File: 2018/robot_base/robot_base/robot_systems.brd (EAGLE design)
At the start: 102.8 x 91.4 mm, 92 parts, among them IC1 DRV8840PWP, IC1_C1 0.01uF, IC1_C2 0.1uF, IC1_C3 0.1uF, IC1_C4 0.1uF, IC1_C5 100uF, IC1_C6 470nF, IC1_R1 ???, IC1_R2 ???, IC1_R3 10k, IC1_R4 100m, IC1_R5 1M, IC2 DRV8840PWP, IC2_C1 0.01uF, IC2_C2 0.1uF, IC2_C3 0.1uF, IC2_C4 0.1uF, IC2_C5 100uF, IC2_C6 470nF, IC2_R1 ???, IC2_R2 ???, IC2_R3 10k, IC2_R4 100m, IC2_R5 1M, IC3 DRV8840PWP, IC3_C1 0.01uF, IC3_C2 0.1uF, IC3_C3 0.1uF, IC3_C4 0.1uF, IC3_C5 100uF, IC3_C6 470nF, IC3_R1 ???, IC3_R2 ???, IC3_R3 10k, IC3_R4 100m, IC3_R5 1M

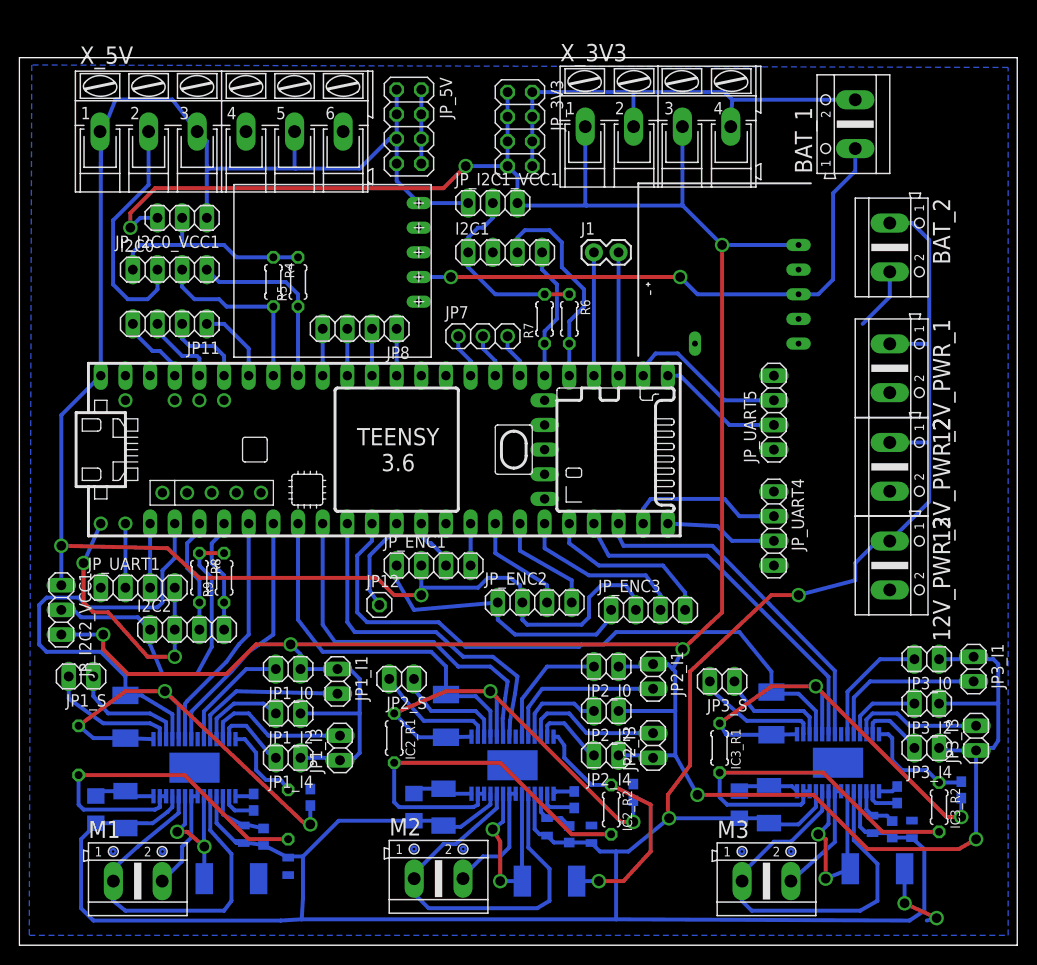
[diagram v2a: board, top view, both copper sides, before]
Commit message: [robot_base] Update robot_base and robot_systems boards.
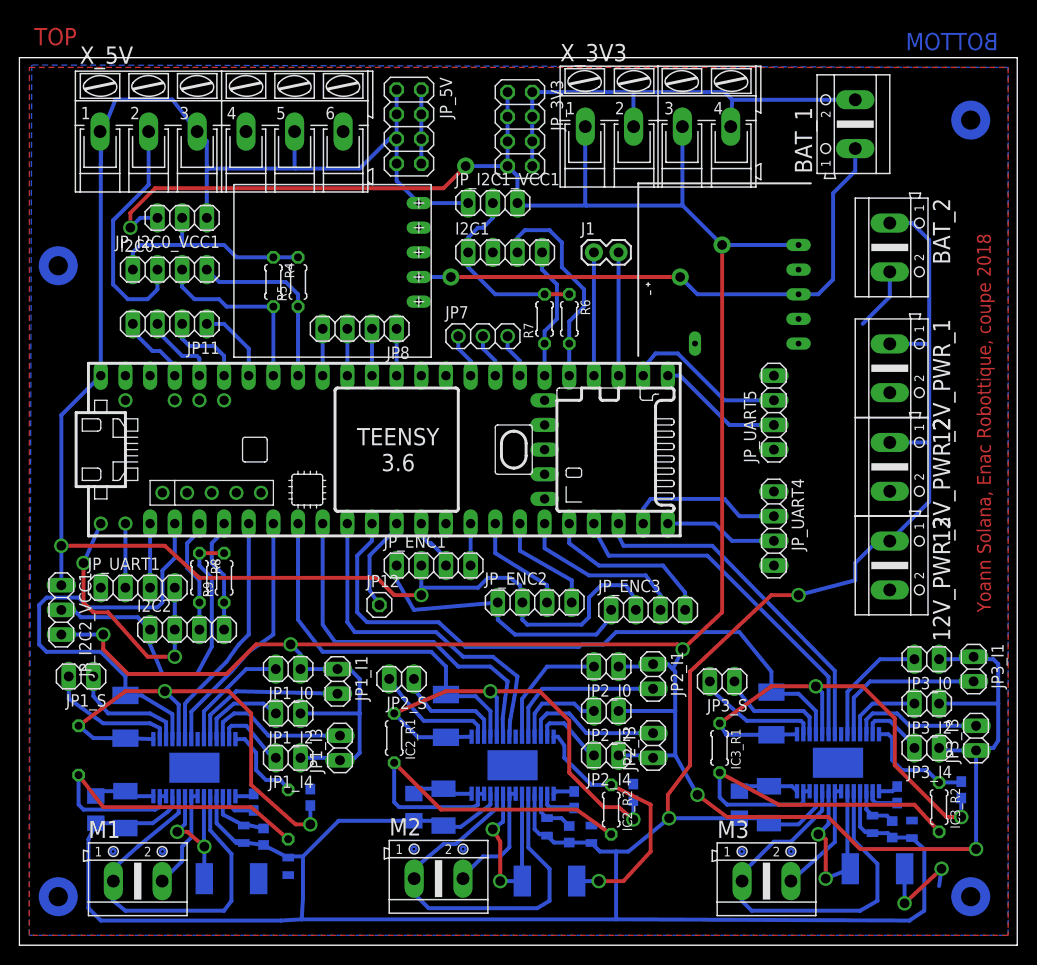
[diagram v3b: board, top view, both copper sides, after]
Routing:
- net IC1_V3P3: track 46.2 -> 51.1 mm
- net IC3_V3P3: track 47.5 -> 50.3 mm
- net IC2_V3P3: track 46.8 -> 49.5 mm
- net GND: track 218.7 -> 221.0 mm
- net 12V2: track 301.8 -> 300.6 mm
- net 3V3: track 347.1 -> 347.7 mm
- added copper zone on layer 1, net GND
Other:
- board text added: "BOTTOM"
- board text added: "TOP"
- board text added: "Yoann Solana, Enac Robottique, coupe 2018"

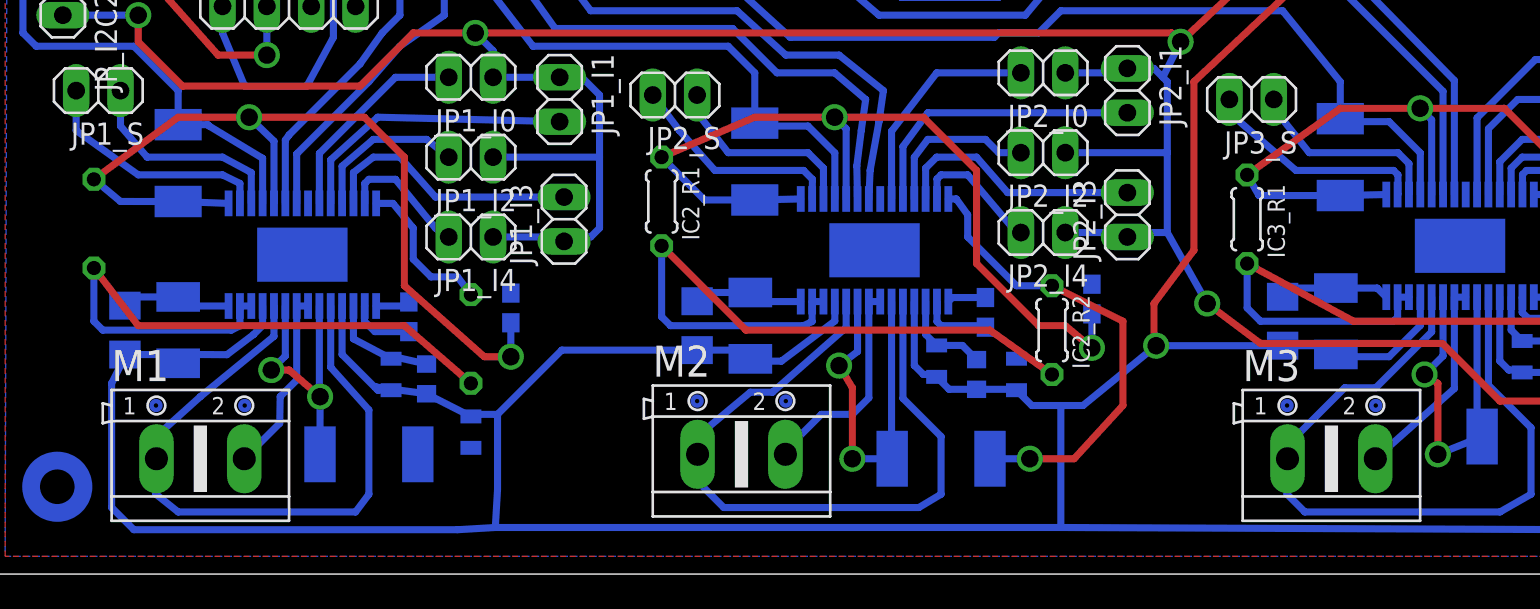
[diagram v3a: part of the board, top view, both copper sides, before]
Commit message: [robot_system] Increase clearance, update package of one condo
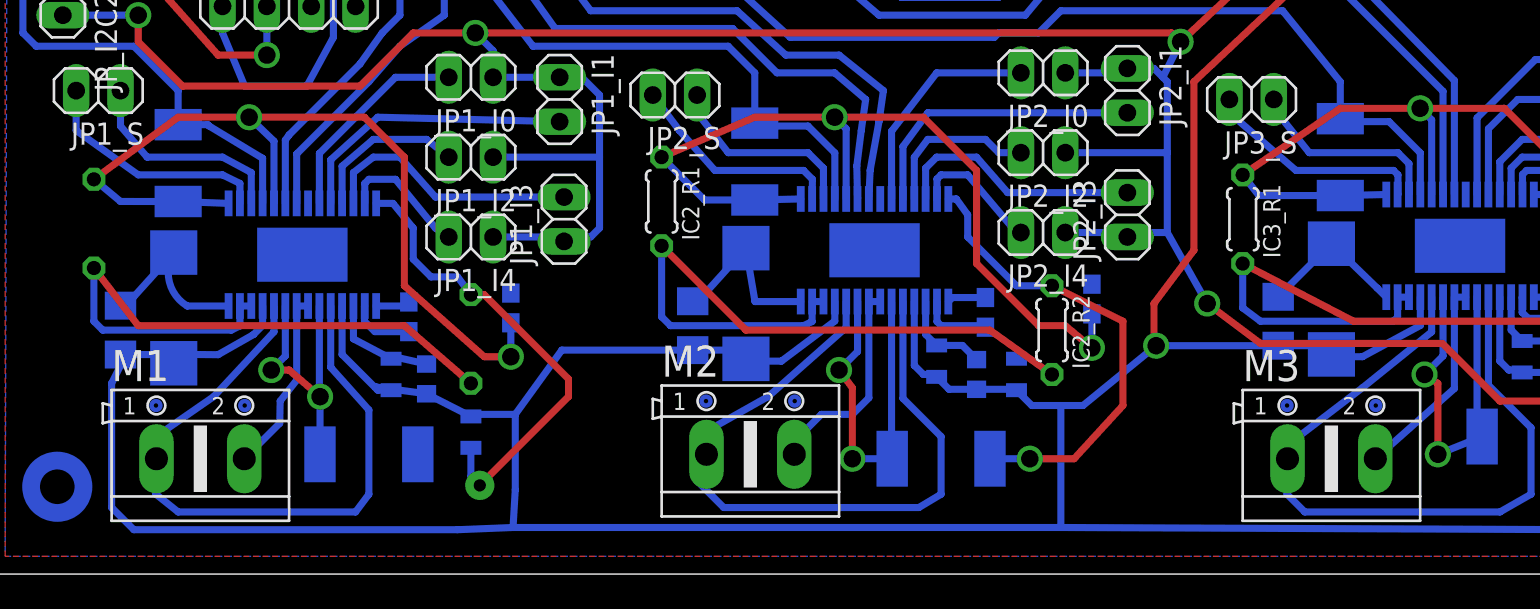
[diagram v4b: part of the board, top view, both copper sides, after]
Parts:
- IC1_C5, IC2_C5, IC3_C5: device SparkFun-Passives:EIA3528-KIT -> SparkFun-Passives:EIA7343
- moved IC2_C5 1.30 mm to (43.4, 15.5)
- moved IC1_C5 1.30 mm to (10.7, 15.2)
- moved IC3_C5 1.30 mm to (77.0, 15.7)
- moved M2 0.51 mm to (43.7, 6.86)
- moved IC3_C4 0.25 mm to (73.9, 14.5)
- moved IC1_C4 0.25 mm to (7.62, 14.0)
- moved IC2_C4 0.25 mm to (40.4, 14.2)
- moved IC3_R1 0.25 mm to (71.9, 20.3)
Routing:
- net GND: track 221.0 -> 248.5 mm, vias 5 -> 6
- net M2_1: track 41.6 -> 42.4 mm
- net 12V2: track 300.6 -> 301.1 mm

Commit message: Debut test motor control
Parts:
- removed 12V_PWR_1, 12V_PWR_2, 12V_PWR_3, BAT_1, BAT_2, M2, M3: (no value), con-ptr500:AK500/2
- removed D24V22F3: D24V22F3, D24V22F3:D24V22F3
- removed D24V50F5: D24V50F5, D24V50F5:D24V50F5
- removed I2C0, I2C1, I2C2, JP11, JP8, JP_ENC1, JP_ENC2, JP_ENC3, JP_UART1, JP_UART4, JP_UART5: (no value), pinhead:1X04
- removed IC2, IC3: DRV8840PWP, DRV8840PWP:SOP65P640X120-29N
- removed IC2_C1, IC3_C1: 0.01uF, rcl:C0603
- removed IC2_C2, IC2_C3, IC3_C2, IC3_C3: 0.1uF, SparkFun-Passives:0805
- removed IC2_C4, IC3_C4: 0.1uF, SparkFun-Passives:1206
- removed IC2_C5, IC3_C5: 100uF, SparkFun-Passives:EIA7343
- removed IC2_C6, IC3_C6: 470nF, rcl:C0603
- removed IC2_R1, IC2_R2, IC3_R1, IC3_R2: ???, resistor:0204/5
- removed IC2_R3, IC3_R3: 10k, rcl:R2010
- removed IC2_R4, IC3_R4: 100m, rcl:R2512
- removed IC2_R5, IC3_R5: 1M, rcl:R0603
- removed J1: (no value), SparkFun-Connectors:1X02
- removed JP12: (no value), pinhead:1X01
- removed JP1_I0, JP1_I1, JP1_I2, JP1_I3, JP1_I4, JP1_S, JP2_I0, JP2_I1, JP2_I2, JP2_I3, JP2_I4, JP2_S, JP3_I0, JP3_I1, JP3_I2, JP3_I3, JP3_I4, JP3_S: (no value), pinhead:1X02
- removed JP7: (no value), adafruit:1X03
- removed JP_3V3, JP_5V: (no value), pinhead:2X04
- removed JP_I2C0_VCC1, JP_I2C1_VCC1, JP_I2C2_VCC1: (no value), pinhead:1X03
- removed R4, R5, R6, R7, R8, R9: (no value), rcl:0204/5
- removed U$1: TEENSY_3.5/3.6TEENSY_3.5/3.6_LONG_PADS, Teensy356:TEENSY_3.5/3.6
- removed X_3V3: (no value), con-ptr500:AK300/4
- removed X_5V: (no value), con-ptr500:AK300/6
- added JP1: (no value), pinhead:1X06
- added JP2: (no value), pinhead:1X04
- added JP3: (no value), pinhead:1X03
- moved M1 11.4 mm to (12.2, -4.83)
- moved IC1_R4 7.40 mm to (23.9, -0.25)
- moved IC1_R2 5.79 mm to (32.3, 9.91)
- moved IC1_C5 5.71 mm to (5.84, 12.2)
- moved IC1_R1 3.87 mm to (4.57, 23.6)
- moved IC1_R3 3.76 mm to (11.8, 27.2), turned to 0 degrees
- moved IC1_C6 3.06 mm to (29.7, 18.3)
- moved IC1_C4 2.79 mm to (10.4, 14.0)
- moved IC1_C2 2.05 mm to (21.1, 11.7)
- moved IC1_C3 1.30 mm to (26.4, 7.87)
- moved IC1_R5 0.57 mm to (24.6, 11.4)
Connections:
- removed net 3V3: D24V22F3.VOUT, JP1_I0.1, JP1_I1.1, JP1_I2.1, JP1_I3.1, JP1_I4.1, JP2_I0.1, JP2_I1.1, JP2_I2.1, JP2_I3.1, JP2_I4.1, JP3_I0.1, JP3_I1.1, JP3_I2.1, JP3_I3.1, JP3_I4.1, JP_3V3.1, JP_3V3.3, JP_3V3.5, JP_3V3.7, JP_I2C0_VCC1.3, JP_I2C1_VCC1.3, JP_I2C2_VCC1.3, X_3V3.1, X_3V3.3
- removed net 5V: D24V50F5.VOUT, JP_5V.1, JP_5V.3, JP_5V.5, JP_5V.7, JP_ENC1.2, JP_ENC2.2, JP_ENC3.2, JP_I2C0_VCC1.1, JP_I2C1_VCC1.1, JP_I2C2_VCC1.1, U$1.VIN, X_5V.1, X_5V.3, X_5V.5
- removed net CUR1_NF: JP11.1, U$1.20/A6
- removed net CUR1_SE: JP8.4, U$1.17/A3
- removed net CUR2_NF: JP8.3, U$1.16/A2
- removed net CUR2_SE: JP8.2, U$1.15/A1
- removed net CUR3_NF: JP8.1, U$1.14/A0
- removed net ENC1_A: JP_ENC1.3, U$1.12/MISO
- removed net ENC1_B: JP_ENC1.4, U$1.24
- removed net ENC2_A: JP_ENC2.3, U$1.25
- removed net ENC2_B: JP_ENC2.4, U$1.26
- removed net ENC3_A: JP_ENC3.3, U$1.27
- removed net ENC3_B: JP_ENC3.4, U$1.28
- removed net I2C0_VCC: I2C0.1, JP_I2C0_VCC1.2, R4.1, R5.2
- removed net I2C1_VCC: I2C1.1, JP_I2C1_VCC1.2, R6.1, R7.2
- removed net I2C2_VCC: I2C2.1, JP_I2C2_VCC1.2, R8.1, R9.2
- removed net IC2_I0: IC2.23, JP2_I0.2
- removed net IC2_I1: IC2.24, JP2_I1.2
- removed net IC2_I2: IC2.25, JP2_I2.2
- removed net IC2_I3: IC2.26, JP2_I3.2
- removed net IC2_I4: IC2.27, JP2_I4.2
- removed net IC2_NFAULT: IC2.18, IC2_R3.1, U$1.7
- removed net IC2_NRESET: IC2.16, JP2_S.2
- removed net IC2_NSLEEP: IC2.17, JP2_S.1
- removed net IC2_V3P3: IC2.15, IC2.19, IC2_C6.1, IC2_R1.1, IC2_R3.2
- removed net IC3_I0: IC3.23, JP3_I0.2
- removed net IC3_I1: IC3.24, JP3_I1.2
- removed net IC3_I2: IC3.25, JP3_I2.2
- removed net IC3_I3: IC3.26, JP3_I3.2
- removed net IC3_I4: IC3.27, JP3_I4.2
- removed net IC3_NFAULT: IC3.18, IC3_R3.1, U$1.10/CS
- removed net IC3_NRESET: IC3.16, JP3_S.2
- removed net IC3_NSLEEP: IC3.17, JP3_S.1
- removed net IC3_R2: IC3.12, IC3.13, IC3_R1.2, IC3_R2.2
- removed net IC3_V3P3: IC3.15, IC3.19, IC3_C6.1, IC3_R1.1, IC3_R3.2
- removed net M2_1: IC2.10, IC2.5, M2.1
- removed net M2_2: IC2.7, IC2.8, M2.2
- removed net M3_1: IC3.10, IC3.5, M3.1
- removed net M3_2: IC3.7, IC3.8, M3.2
- removed net MOT2_DIR: IC2.20, U$1.8
- removed net MOT2_PWM: IC2.21, U$1.9/CS
- removed net MOT3_DIR: IC3.20, U$1.29
- removed net MOT3_PWM: IC3.21, U$1.30
- removed net N$1: JP11.4, U$1.23/A9
- removed net N$13: IC2.1, IC2_C1.1
- removed net N$14: IC2.2, IC2_C1.2
- removed net N$15: IC2.3, IC2_C2.2, IC2_R5.2
- removed net N$17: IC3.6, IC3.9, IC3_R4.2
- removed net N$18: IC3.1, IC3_C1.1
- removed net N$19: IC3.2, IC3_C1.2
- removed net N$20: IC3.3, IC3_C2.2, IC3_R5.2
- removed net N$3: IC2.12, IC2.13, IC2_R1.2, IC2_R2.2
- removed net N$4: JP11.3, U$1.22/A8
- removed net N$52: JP7.1, U$1.A22/DAC1
- removed net N$53: JP7.2, U$1.21/DAC0
- removed net N$57: J1.1, U$1.36/A17
- removed net N$58: J1.2, U$1.35/A16
- removed net N$6: JP11.2, U$1.21/A7
- removed net N$7: JP12.1, U$1.11/MOSI
- removed net N$8: BAT_1.1, D24V22F3.VIN, D24V50F5.VIN
- removed net N$9: IC2.6, IC2.9, IC2_R4.2
- removed net NS50: JP7.3, U$1.39/A20
- removed net RX1: JP_UART1.2, U$1.0/RX
- removed net RX4: JP_UART4.2, U$1.31/A12
- removed net RX5: JP_UART5.3, U$1.34/A15
- removed net SCL0: I2C0.3, R4.2, U$1.19/A5/SCL
- removed net SCL1: I2C1.3, R6.2, U$1.37/A18
- removed net SCL2: I2C2.3, R8.2, U$1.3/CANTX
- removed net SDA0: I2C0.4, R5.1, U$1.18/A4/SDA
- removed net SDA1: I2C1.4, R7.1, U$1.38/A19
- removed net SDA2: I2C2.4, R9.1, U$1.4/CANRX
- removed net TX1: JP_UART1.3, U$1.1/TX
- removed net TX4: JP_UART4.3, U$1.32/A13
- removed net TX5: JP_UART5.2, U$1.33/A14
- new net DECAY: IC1.19, JP2.4
- net 12V2: no longer 12V_PWR_1.1, 12V_PWR_2.1, 12V_PWR_3.1, BAT_2.1, IC2.11, IC2.4, IC2_C2.1, IC2_C3.2, IC2_C4.2, IC2_C5.A, IC2_R5.1, IC3.11, IC3.4, IC3_C2.1, IC3_C3.2, IC3_C4.2, IC3_C5.A, IC3_R5.1
- net GND: now also JP1.1, JP2.1, JP3.1; no longer 12V_PWR_1.2, 12V_PWR_2.2, 12V_PWR_3.2, BAT_1.2, BAT_2.2, D24V22F3.GND, D24V22F3.GND_2, D24V22F3.PG, D24V50F5.GND, D24V50F5.GND_2, I2C0.2, I2C1.2, I2C2.2, IC2.14, IC2.28, IC2.29, IC2_C3.1, IC2_C4.1, IC2_C5.C, IC2_C6.2, IC2_R2.1, IC2_R4.1, IC3.14, IC3.28, IC3.29, IC3_C3.1, IC3_C4.1, IC3_C5.C, IC3_C6.2, IC3_R2.1, IC3_R4.1, JP_3V3.2, JP_3V3.4, JP_3V3.6, JP_3V3.8, JP_5V.2, JP_5V.4, JP_5V.6, JP_5V.8, JP_ENC1.1, JP_ENC2.1, JP_ENC3.1, JP_UART1.4, JP_UART4.4, JP_UART5.1, U$1.AGND, U$1.GND, U$1.GND2, X_3V3.2, X_3V3.4, X_5V.2, X_5V.4, X_5V.6
- net IC1_I0: now also JP1.6; no longer JP1_I0.2
- net IC1_I1: now also JP1.5; no longer JP1_I1.2
- net IC1_I2: now also JP1.4; no longer JP1_I2.2
- net IC1_I3: now also JP1.3; no longer JP1_I3.2
- net IC1_I4: now also JP1.2; no longer JP1_I4.2
- net IC1_NFAULT: no longer U$1.2
- net IC1_NRESET: now also JP3.3; no longer JP1_S.2
- net IC1_NSLEEP: now also JP3.2; no longer JP1_S.1
- net IC1_V3P3: no longer IC1.19
- net MOT1_DIR: now also JP2.3; no longer U$1.5
- net MOT1_PWM: now also JP2.2; no longer U$1.6
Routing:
- net 3V3: track 347.7 -> 0.00 mm, vias 8 -> 0
- net 12V2: track 301.1 -> 13.8 mm, vias 2 -> 0
- net GND: track 248.5 -> 19.3 mm, vias 6 -> 0
- net 5V: track 191.1 -> 0.00 mm, vias 2 -> 0
- net IC3_NFAULT: track 66.3 -> 0.00 mm
- net N$8: track 58.5 -> 0.00 mm, vias 2 -> 0
- net IC3_V3P3: track 50.7 -> 0.00 mm, vias 2 -> 0
- net IC2_V3P3: track 49.5 -> 0.00 mm, vias 2 -> 0
- net IC1_V3P3: track 51.1 -> 7.88 mm, vias 2 -> 0
- net M2_1: track 42.4 -> 0.00 mm
- net M3_1: track 42.3 -> 0.00 mm
- net N$3: track 39.9 -> 0.00 mm
- net IC1_NFAULT: track 46.5 -> 6.77 mm
- net M1_1: track 38.6 -> 0.00 mm
- net IC3_R2: track 38.5 -> 0.00 mm
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- removed copper zone on layer 1, net GND
- removed copper zone on layer 16, net GND
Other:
- board outline removed
- board text removed: "Yoann Solana, Enac Robottique, coupe 2018"
